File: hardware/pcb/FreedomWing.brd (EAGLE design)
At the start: 63.2 x 33 mm, 12 parts

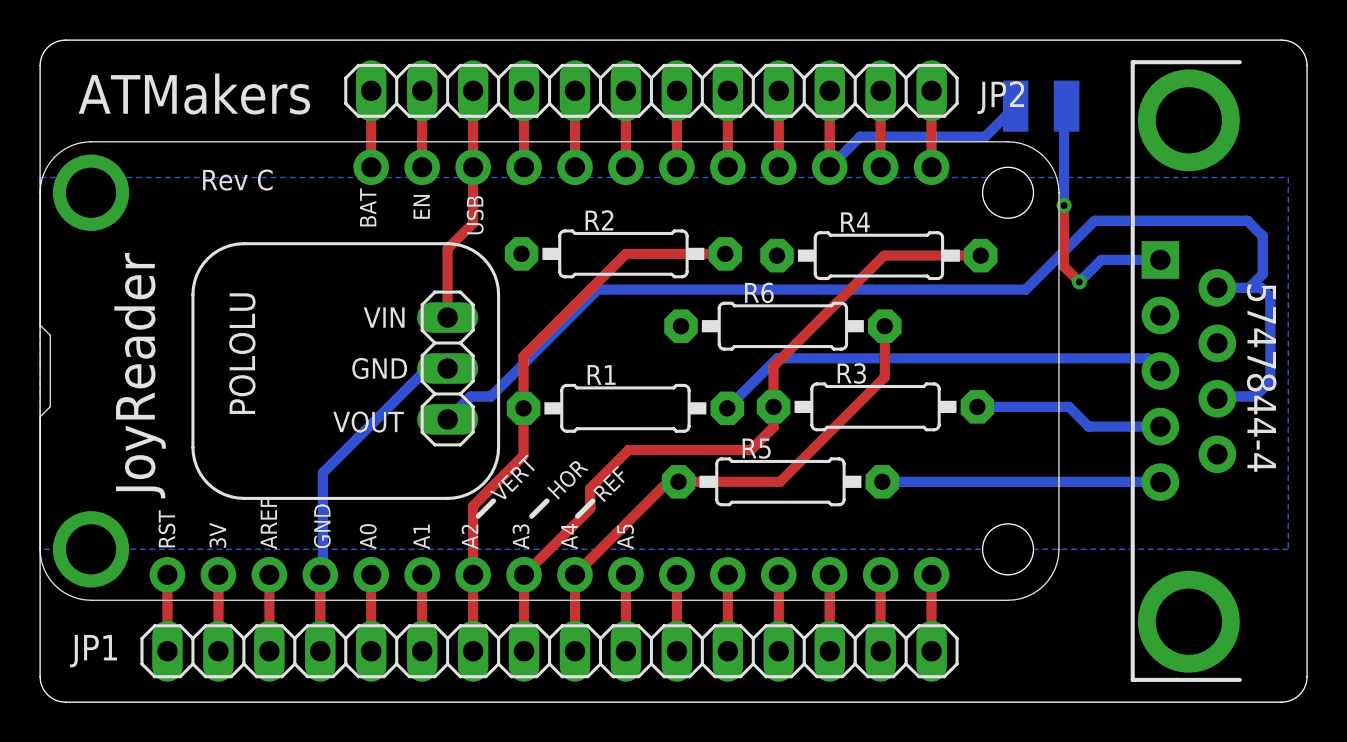
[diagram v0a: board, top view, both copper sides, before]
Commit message: First changes after Launch
Updated to add Schottky Diodes, Reset Switch & Jumper
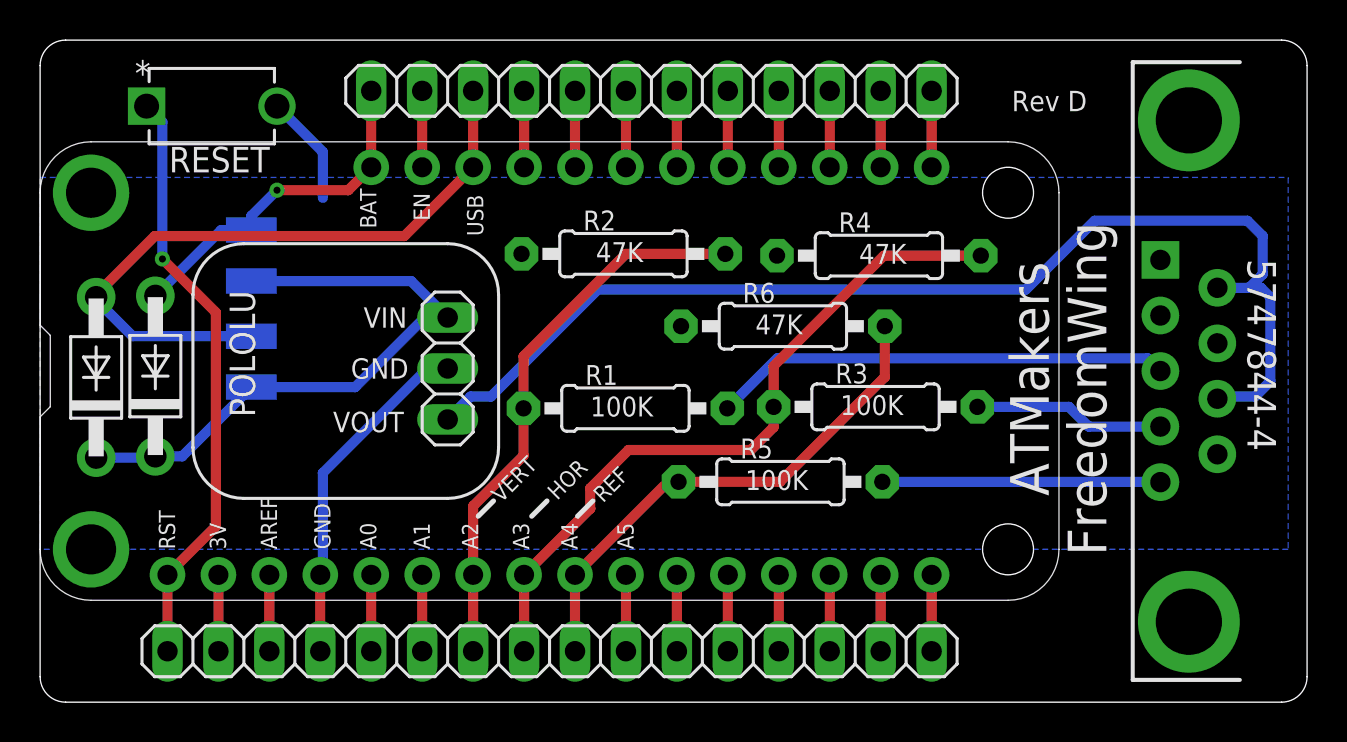
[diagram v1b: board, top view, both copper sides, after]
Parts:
- removed SJ1: (no value), jumper:SJW
- added D1, D2: (no value), adafruit:DO41-7
- added RESET: 1825966-1, ATMakers:SWDIP2_256X170P100
- added USB, VBAT: (no value), jumper:SJW
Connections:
- removed net N$28: JP1.1, MS1.1
- removed net N$8: J2.5, SJ1.1
- new net RESET: JP1.1, MS1.1, RESET.1
- new net VMAX: D1.C, D2.C, POLOLU.1, USB.1, VBAT.1
- net GND: now also RESET.2
- net N$4: no longer SJ1.2
- net USB: now also D1.A, USB.2; no longer POLOLU.1
- net VBAT: now also D2.A, VBAT.2
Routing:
- net VMAX: track 0.00 -> 31.7 mm
- net RESET: track 0.00 -> 29.6 mm, vias 0 -> 1
- net USB: track 11.8 -> 34.0 mm
- net VBAT: track 3.81 -> 17.6 mm, vias 0 -> 1
- net N$8: track 13.6 -> 0.00 mm, vias 2 -> 0
- net N$4: track 14.3 -> 3.81 mm
- net GND: track 17.3 -> 22.8 mm
- net N$28: track 3.81 -> 0.00 mm
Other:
- board text added: "FreedomWing"
- board text added: "Rev D"
- board text added: "w/AbleGamers & GRA-V"
- board text removed: "JoyReader"
- board text removed: "Rev 1.0"
- board text removed: "Rev C"
